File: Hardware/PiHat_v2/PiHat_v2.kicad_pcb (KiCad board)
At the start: 2 copper layers, 64 x 55 mm, 19 parts, among them P1 CONN_02X20, P2 CONN_01X02, P3 CONN_01X08

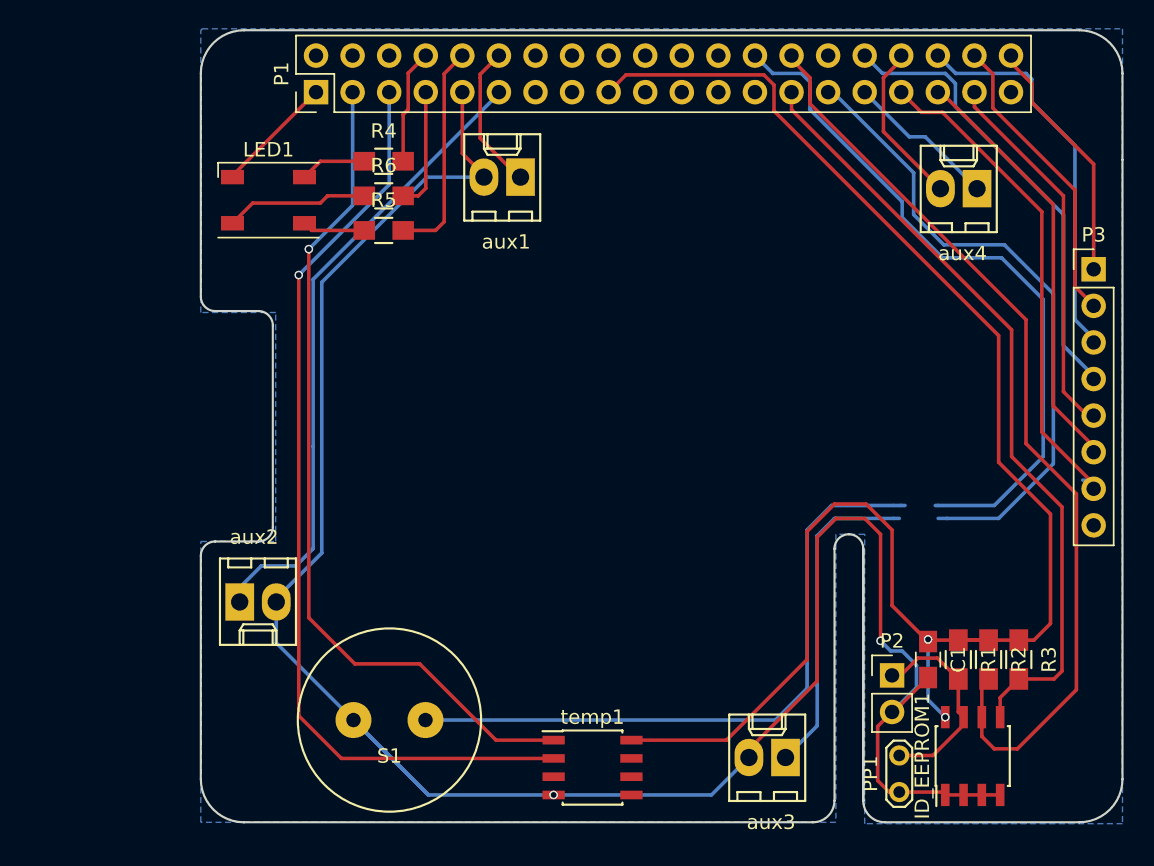
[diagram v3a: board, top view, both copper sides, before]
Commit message: Complete Ground Plane and Keepout Zones
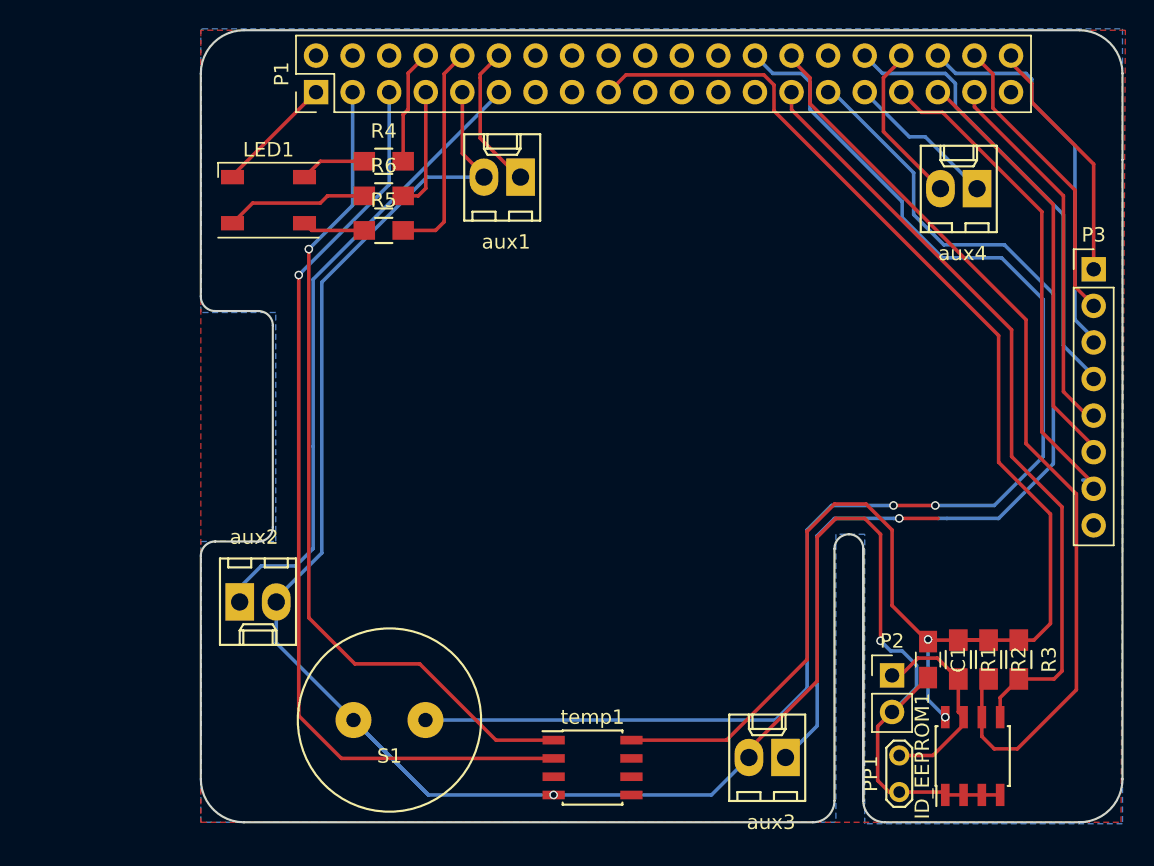
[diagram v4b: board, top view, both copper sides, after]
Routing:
- net /GPIO5: track 67.0 -> 69.7 mm, vias 0 -> 1
- net /GPIO7: track 94.5 -> 96.6 mm, vias 0 -> 2
- added copper zone on F.Cu, net GND
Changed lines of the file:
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@@
   (general
     (links 56)
-    (no_connects 10)
+    (no_connects 9)
     (area 79.650001 53.1 168.85 129.200001)
     (thickness 1.6)
     (drawings 48)
-    (tracks 242)
+    (tracks 245)
     (zones 0)
     (modules 19)
@@
     (38 B.Mask user)
     (39 F.Mask user)
-    (40 Dwgs.User user hide)
+    (40 Dwgs.User user)
     (41 Cmts.User user)
     (42 Eco1.User user)
@@
   (segment (start 113.4 65.06) (end 114.7 63.76) (width 0.25) (layer F.Cu) (net 10))
   (segment (start 116.2 72.2) (end 116.1 72.2) (width 0.25) (layer F.Cu) (net 10))
-  (segment (start 109.6 109.9) (end 133.9 109.9) (width 0.25) (layer B.Cu) (net 20))
-  (segment (start 133.72 65) (end 132.48 63.76) (width 0.25) (layer B.Cu) (net 20))
+  (via (at 142.1 95) (size 0.6) (drill 0.4) (layers F.Cu B.Cu) (net 20))
+  (segment (start 133.9 109.9) (end 136.1 107.7) (width 0.25) (layer B.Cu) (net 20))
+  (segment (start 136.1 107.7) (end 136.1 96.7) (width 0.25) (layer B.Cu) (net 20))
+  (segment (start 136.1 96.7) (end 137.8 95) (width 0.25) (layer B.Cu) (net 20))
+  (segment (start 145.2 95) (end 149.1 95) (width 0.25) (layer B.Cu) (net 20))
+  (segment (start 145 95) (end 145.2 95) (width 0.25) (layer B.Cu) (net 20))
+  (segment (start 137.8 95) (end 142.1 95) (width 0.25) (layer B.Cu) (net 20))
+  (segment (start 149.1 95) (end 152.5 91.6) (width 0.25) (layer B.Cu) (net 20))
+  (segment (start 152.5 91.6) (end 152.5 80.7) (width 0.25) (layer B.Cu) (net 20))
+  (segment (start 152.5 80.7) (end 149.6 77.8) (width 0.25) (layer B.Cu) (net 20))
+  (segment (start 149.6 77.8) (end 145.5 77.8) (width 0.25) (layer B.Cu) (net 20))
+  (segment (start 145.5 77.8) (end 142.7 75) (width 0.25) (layer B.Cu) (net 20))
+  (segment (start 142.7 75) (end 142.7 73.9) (width 0.25) (layer B.Cu) (net 20))
+  (segment (start 142.7 73.9) (end 136.3 67.5) (width 0.25) (layer B.Cu) (net 20))
+  (segment (start 136.3 67.5) (end 136.3 65.6) (width 0.25) (layer B.Cu) (net 20))
+  (segment (start 136.3 65.6) (end 135.7 65) (width 0.25) (layer B.Cu) (net 20))
   (segment (start 135.7 65) (end 133.72 65) (width 0.25) (layer B.Cu) (net 20))
-  (segment (start 136.3 65.6) (end 135.7 65) (width 0.25) (layer B.Cu) (net 20))
-  (segment (start 136.3 67.5) (end 136.3 65.6) (width 0.25) (layer B.Cu) (net 20))
-  (segment (start 142.7 73.9) (end 136.3 67.5) (width 0.25) (layer B.Cu) (net 20))
-  (segment (start 142.7 75) (end 142.7 73.9) (width 0.25) (layer B.Cu) (net 20))
-  (segment (start 145.5 77.8) (end 142.7 75) (width 0.25) (layer B.Cu) (net 20))
-  (segment (start 149.6 77.8) (end 145.5 77.8) (width 0.25) (layer B.Cu) (net 20))
-  (segment (start 152.5 80.7) (end 149.6 77.8) (width 0.25) (layer B.Cu) (net 20))
-  (segment (start 152.5 91.6) (end 152.5 80.7) (width 0.25) (layer B.Cu) (net 20))
-  (segment (start 149.1 95) (end 152.5 91.6) (width 0.25) (layer B.Cu) (net 20))
-  (segment (start 137.8 95) (end 142.1 95) (width 0.25) (layer B.Cu) (net 20))
-  (segment (start 142.1 95) (end 142.6 95) (width 0.25) (layer B.Cu) (net 20))
-  (segment (start 142.6 95) (end 142.9 95) (width 0.25) (layer B.Cu) (net 20))
-  (segment (start 145 95) (end 145.2 95) (width 0.25) (layer B.Cu) (net 20))
-  (segment (start 145.2 95) (end 149.1 95) (width 0.25) (layer B.Cu) (net 20))
-  (segment (start 136.1 96.7) (end 137.8 95) (width 0.25) (layer B.Cu) (net 20))
-  (segment (start 136.1 107.7) (end 136.1 96.7) (width 0.25) (layer B.Cu) (net 20))
-  (segment (start 133.9 109.9) (end 136.1 107.7) (width 0.25) (layer B.Cu) (net 20))
+  (segment (start 132.48 63.76) (end 133.72 65) (width 0.25) (layer B.Cu) (net 20))
+  (segment (start 133.9 109.9) (end 109.6 109.9) (width 0.25) (layer B.Cu) (net 20))
+  (via (at 145 95) (size 0.6) (drill 0.4) (layers F.Cu B.Cu) (net 20))
+  (segment (start 142.1 95) (end 145 95) (width 0.25) (layer F.Cu) (net 20))
   (segment (start 150.8 107.05) (end 153.25 107.05) (width 0.25) (layer F.Cu) (net 21))
   (segment (start 135.02 67.52) (end 135.02 66.3) (width 0.25) (layer F.Cu) (net 21))
@@
   (segment (start 149.1 111.9) (end 148.235 111.035) (width 0.25) (layer F.Cu) (net 22))
   (segment (start 148.235 111.035) (end 148.235 109.7) (width 0.25) (layer F.Cu) (net 22))
+  (via (at 142.5 95.9) (size 0.6) (drill 0.4) (layers F.Cu B.Cu) (net 23))
+  (segment (start 136.8 97.1) (end 136.8 107.5) (width 0.25) (layer B.Cu) (net 23))
+  (segment (start 138 95.9) (end 136.8 97.1) (width 0.25) (layer B.Cu) (net 23))
+  (segment (start 142.5 95.9) (end 142.1 95.9) (width 0.25) (layer B.Cu) (net 23))
+  (segment (start 142.1 95.9) (end 138 95.9) (width 0.25) (layer B.Cu) (net 23))
+  (segment (start 134.6 112.5) (end 136.8 110.3) (width 0.25) (layer B.Cu) (net 23))
   (segment (start 136.8 107.5) (end 136.8 110.3) (width 0.25) (layer B.Cu) (net 23))
-  (segment (start 136.8 110.3) (end 134.6 112.5) (width 0.25) (layer B.Cu) (net 23))
+  (segment (start 142.5 95.9) (end 145.2 95.9) (width 0.25) (layer F.Cu) (net 23))
   (segment (start 137.9 66.3) (end 143.5 71.9) (width 0.25) (layer B.Cu) (net 23))
   (segment (start 143.5 71.9) (end 143.5 74.8) (width 0.25) (layer B.Cu) (net 23))
@@
   (segment (start 153.2 80.3) (end 153.2 92.1) (width 0.25) (layer B.Cu) (net 23))
   (segment (start 153.2 92.1) (end 149.4 95.9) (width 0.25) (layer B.Cu) (net 23))
-  (segment (start 142.1 95.9) (end 138 95.9) (width 0.25) (layer B.Cu) (net 23))
-  (segment (start 142.5 95.9) (end 142.1 95.9) (width 0.25) (layer B.Cu) (net 23))
   (segment (start 149.4 95.9) (end 145.8 95.9) (width 0.25) (layer B.Cu) (net 23))
   (segment (start 145.8 95.9) (end 145.2 95.9) (width 0.25) (layer B.Cu) (net 23))
-  (segment (start 138 95.9) (end 136.8 97.1) (width 0.25) (layer B.Cu) (net 23))
-  (segment (start 136.8 97.1) (end 136.8 107.5) (width 0.25) (layer B.Cu) (net 23))
   (segment (start 137.56 66.3) (end 137.9 66.3) (width 0.25) (layer B.Cu) (net 23))
   (segment (start 140.1 66.3) (end 143.2 69.4) (width 0.25) (layer B.Cu) (net 24))
@@
       )
     )
+  )
+  (zone (net 0) (net_name "") (layer F.Cu) (hatch edge 0.508)
+    (connect_pads (clearance 0.508))
+    (min_thickness 0.254)
+    (keepout (tracks not_allowed) (vias not_allowed) (copperpour not_allowed))
+    (fill (arc_segments 16) (thermal_gap 0.508) (thermal_bridge_width 0.508))
+    (polygon
+      (pts
+        (xy 157.9 110.4) (xy 155 110.4) (xy 153.2 110.4) (xy 151.5 112.1) (xy 151.5 116.4)
+        (xy 158 116.4) (xy 158 110.4)
+      )
+    )
+  )
+  (zone (net 0) (net_name "") (layer B.Cu) (hatch edge 0.508)
+    (connect_pads (clearance 0.508))
+    (min_thickness 0.254)
+    (keepout (tracks not_allowed) (vias not_allowed) (copperpour not_allowed))
+    (fill (arc_segments 16) (thermal_gap 0.508) (thermal_bridge_width 0.508))
+    (polygon
+      (pts
+        (xy 158 110.6) (xy 152.5 110.6) (xy 151.5 111.6) (xy 151.5 117.1) (xy 158 117.1)
+      )
+    )
+  )
+  (zone (net 0) (net_name "") (layer B.Cu) (hatch edge 0.508)
+    (connect_pads (clearance 0.508))
+    (min_thickness 0.254)
+    (keepout (tracks not_allowed) (vias not_allowed) (copperpour not_allowed))
+    (fill (arc_segments 16) (thermal_gap 0.508) (thermal_bridge_width 0.508))
+    (polygon
+      (pts
+        (xy 100.4 67.1) (xy 99.2 68.3) (xy 94 68.3) (xy 94 62) (xy 100.4 62)
+      )
+    )
+  )
+  (zone (net 0) (net_name "") (layer F.Cu) (hatch edge 0.508)
+    (connect_pads (clearance 0.508))
+    (min_thickness 0.254)
+    (keepout (tracks not_allowed) (vias not_allowed) (copperpour not_allowed))
+    (fill (arc_segments 16) (thermal_gap 0.508) (thermal_bridge_width 0.508))
+    (polygon
+      (pts
+        (xy 100.4 67.1) (xy 99.2 68.3) (xy 94 68.3) (xy 94 61.9) (xy 100.4 61.9)
+      )
+    )
+  )
+  (zone (net 0) (net_name "") (layer B.Cu) (hatch edge 0.508)
+    (connect_pads (clearance 0.508))
+    (min_thickness 0.254)
+    (keepout (tracks not_allowed) (vias not_allowed) (copperpour not_allowed))
+    (fill (arc_segments 16) (thermal_gap 0.508) (thermal_bridge_width 0.508))
+    (polygon
+      (pts
+        (xy 100.3 116.9) (xy 94 116.9) (xy 94 110.7) (xy 100.3 110.7)
+      )
+    )
+  )
+  (zone (net 0) (net_name "") (layer F.Cu) (hatch edge 0.508)
+    (connect_pads (clearance 0.508))
+    (min_thickness 0.254)
+    (keepout (tracks not_allowed) (vias not_allowed) (copperpour not_allowed))
+    (fill (arc_segments 16) (thermal_gap 0.508) (thermal_bridge_width 0.508))
+    (polygon
+      (pts
+        (xy 100.3 110.7) (xy 94 110.7) (xy 94 117) (xy 100.3 117) (xy 100.3 113.4)
+      )
+    )
+  )
+  (zone (net 2) (net_name GND) (layer F.Cu) (hatch edge 0.508)
+    (connect_pads (clearance 0.508))
+    (min_thickness 0.254)
+    (fill yes (arc_segments 16) (thermal_gap 0.508) (thermal_bridge_width 0.508) (smoothing chamfer))
+    (polygon
+      (pts
+        (xy 158.2 62) (xy 94 62) (xy 94 117) (xy 157.9 117)
+      )
+    )

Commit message: Implement Mounting Holes & Remove Improper Keepout Areas
This board should be electrically sound - and looks to me like it has
all the right parts at first glance. There are some definite silk-screen
improvements that can be made, however.
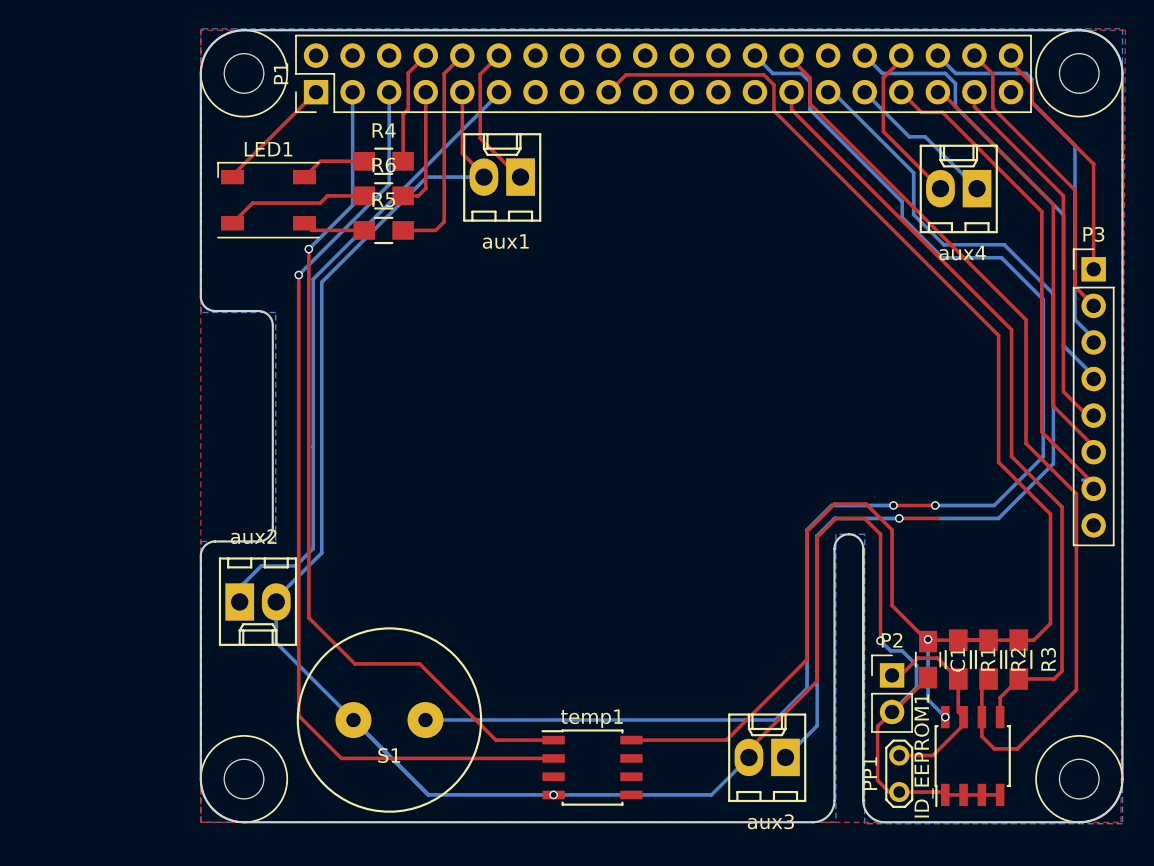
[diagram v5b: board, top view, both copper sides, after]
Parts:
- added REF**: Mounting Hole, .pretty:raspiMountingHole, F.Cu at (97.0, 65.0)
- added REF**: Mounting Hole, .pretty:raspiMountingHole, F.Cu at (97.0, 114.0)
- added REF**: Mounting Hole, .pretty:raspiMountingHole, F.Cu at (155.0, 114.0)
- added REF**: Mounting Hole, .pretty:raspiMountingHole, F.Cu at (155.0, 65.0)
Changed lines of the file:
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@@
     (tracks 245)
     (zones 0)
-    (modules 19)
+    (modules 23)
     (nets 41)
   )
@@
     (38 B.Mask user)
     (39 F.Mask user)
-    (40 Dwgs.User user)
+    (40 Dwgs.User user hide)
     (41 Cmts.User user)
     (42 Eco1.User user)
@@
       (rotate (xyz 0 0 0))
     )
+  )
+  (module .pretty:raspiMountingHole (layer F.Cu)
+    (at 97 65)
+    (descr "module 1 pin (ou trou mecanique de percage)")
+    (tags DEV)
+    (fp_text reference REF** (at 0 -3.048) (layer F.SilkS) hide
+      (effects (font (size 1 1) (thickness 0.15)))
+    )
+    (fp_text value "Mounting Hole" (at 0 3) (layer F.Fab)
+      (effects (font (size 1 1) (thickness 0.15)))
+    )
+    (fp_circle (center 0 0) (end 2.75 0.8) (layer F.Fab) (width 0.1))
+    (fp_circle (center 0 0) (end 3.1 0) (layer F.CrtYd) (width 0.05))
+    (fp_circle (center 0 0) (end 0 -3) (layer F.SilkS) (width 0.12))
+    (pad "" np_thru_hole circle (at 0 0) (size 2.75 2.75) (drill 2.75) (layers *.Cu *.Mask)
+      (clearance 3.1))
+  )
+  (module .pretty:raspiMountingHole (layer F.Cu)
+    (at 97 114)
+    (descr "module 1 pin (ou trou mecanique de percage)")
+    (tags DEV)
+    (fp_text reference REF** (at 0 -3.048) (layer F.SilkS) hide
+      (effects (font (size 1 1) (thickness 0.15)))
+    )
+    (fp_text value "Mounting Hole" (at 0 3) (layer F.Fab)
+      (effects (font (size 1 1) (thickness 0.15)))
+    )
+    (fp_circle (center 0 0) (end 2.75 0.8) (layer F.Fab) (width 0.1))
+    (fp_circle (center 0 0) (end 3.1 0) (layer F.CrtYd) (width 0.05))
+    (fp_circle (center 0 0) (end 0 -3) (layer F.SilkS) (width 0.12))
+    (pad "" np_thru_hole circle (at 0 0) (size 2.75 2.75) (drill 2.75) (layers *.Cu *.Mask)
+      (clearance 3.1))
+  )
+  (module .pretty:raspiMountingHole (layer F.Cu)
+    (at 155 114)
+    (descr "module 1 pin (ou trou mecanique de percage)")
+    (tags DEV)
+    (fp_text reference REF** (at 0 -3.048) (layer F.SilkS) hide
+      (effects (font (size 1 1) (thickness 0.15)))
+    )
+    (fp_text value "Mounting Hole" (at 0 3) (layer F.Fab)
+      (effects (font (size 1 1) (thickness 0.15)))
+    )
+    (fp_circle (center 0 0) (end 2.75 0.8) (layer F.Fab) (width 0.1))
+    (fp_circle (center 0 0) (end 3.1 0) (layer F.CrtYd) (width 0.05))
+    (fp_circle (center 0 0) (end 0 -3) (layer F.SilkS) (width 0.12))
+    (pad "" np_thru_hole circle (at 0 0) (size 2.75 2.75) (drill 2.75) (layers *.Cu *.Mask)
+      (clearance 3.1))
+  )
+  (module .pretty:raspiMountingHole (layer F.Cu)
+    (at 155 65)
+    (descr "module 1 pin (ou trou mecanique de percage)")
+    (tags DEV)
+    (fp_text reference REF** (at 0 -3.048) (layer F.SilkS) hide
+      (effects (font (size 1 1) (thickness 0.15)))
+    )
+    (fp_text value "Mounting Hole" (at 0 3) (layer F.Fab)
+      (effects (font (size 1 1) (thickness 0.15)))
+    )
+    (fp_circle (center 0 0) (end 2.75 0.8) (layer F.Fab) (width 0.1))
+    (fp_circle (center 0 0) (end 3.1 0) (layer F.CrtYd) (width 0.05))
+    (fp_circle (center 0 0) (end 0 -3) (layer F.SilkS) (width 0.12))
+    (pad "" np_thru_hole circle (at 0 0) (size 2.75 2.75) (drill 2.75) (layers *.Cu *.Mask)
+      (clearance 3.1))
   )
   (gr_line (start 136.5 117) (end 97 117) (angle 90) (layer Edge.Cuts) (width 0.15))
@@
       )
     )
-  )
-  (zone (net 0) (net_name "") (layer F.Cu) (hatch edge 0.508)
-    (connect_pads (clearance 0.508))
-    (min_thickness 0.254)
-    (keepout (tracks not_allowed) (vias not_allowed) (copperpour not_allowed))
-    (fill (arc_segments 16) (thermal_gap 0.508) (thermal_bridge_width 0.508))
-    (polygon
-      (pts
-        (xy 157.9 110.4) (xy 155 110.4) (xy 153.2 110.4) (xy 151.5 112.1) (xy 151.5 116.4)
-        (xy 158 116.4) (xy 158 110.4)
-      )
-    )
-  )
-  (zone (net 0) (net_name "") (layer B.Cu) (hatch edge 0.508)
-    (connect_pads (clearance 0.508))
-    (min_thickness 0.254)
-    (keepout (tracks not_allowed) (vias not_allowed) (copperpour not_allowed))
-    (fill (arc_segments 16) (thermal_gap 0.508) (thermal_bridge_width 0.508))
-    (polygon
-      (pts
-        (xy 158 110.6) (xy 152.5 110.6) (xy 151.5 111.6) (xy 151.5 117.1) (xy 158 117.1)
-      )
-    )
-  )
-  (zone (net 0) (net_name "") (layer B.Cu) (hatch edge 0.508)
-    (connect_pads (clearance 0.508))
-    (min_thickness 0.254)
-    (keepout (tracks not_allowed) (vias not_allowed) (copperpour not_allowed))
-    (fill (arc_segments 16) (thermal_gap 0.508) (thermal_bridge_width 0.508))
-    (polygon
-      (pts
-        (xy 100.4 67.1) (xy 99.2 68.3) (xy 94 68.3) (xy 94 62) (xy 100.4 62)
-      )
-    )
-  )
-  (zone (net 0) (net_name "") (layer F.Cu) (hatch edge 0.508)
-    (connect_pads (clearance 0.508))
-    (min_thickness 0.254)
-    (keepout (tracks not_allowed) (vias not_allowed) (copperpour not_allowed))
-    (fill (arc_segments 16) (thermal_gap 0.508) (thermal_bridge_width 0.508))
-    (polygon
-      (pts
-        (xy 100.4 67.1) (xy 99.2 68.3) (xy 94 68.3) (xy 94 61.9) (xy 100.4 61.9)
-      )
-    )
-  )
-  (zone (net 0) (net_name "") (layer B.Cu) (hatch edge 0.508)
-    (connect_pads (clearance 0.508))
-    (min_thickness 0.254)
-    (keepout (tracks not_allowed) (vias not_allowed) (copperpour not_allowed))
-    (fill (arc_segments 16) (thermal_gap 0.508) (thermal_bridge_width 0.508))
-    (polygon
-      (pts
-        (xy 100.3 116.9) (xy 94 116.9) (xy 94 110.7) (xy 100.3 110.7)
-      )
-    )
-  )
-  (zone (net 0) (net_name "") (layer F.Cu) (hatch edge 0.508)
-    (connect_pads (clearance 0.508))
-    (min_thickness 0.254)
-    (keepout (tracks not_allowed) (vias not_allowed) (copperpour not_allowed))
-    (fill (arc_segments 16) (thermal_gap 0.508) (thermal_bridge_width 0.508))
-    (polygon
-      (pts
-        (xy 100.3 110.7) (xy 94 110.7) (xy 94 117) (xy 100.3 117) (xy 100.3 113.4)
-      )
-    )
